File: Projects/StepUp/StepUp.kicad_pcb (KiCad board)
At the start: 2 copper layers, 2 parts, among them U1 TMC2300-LA, U2 RP2040

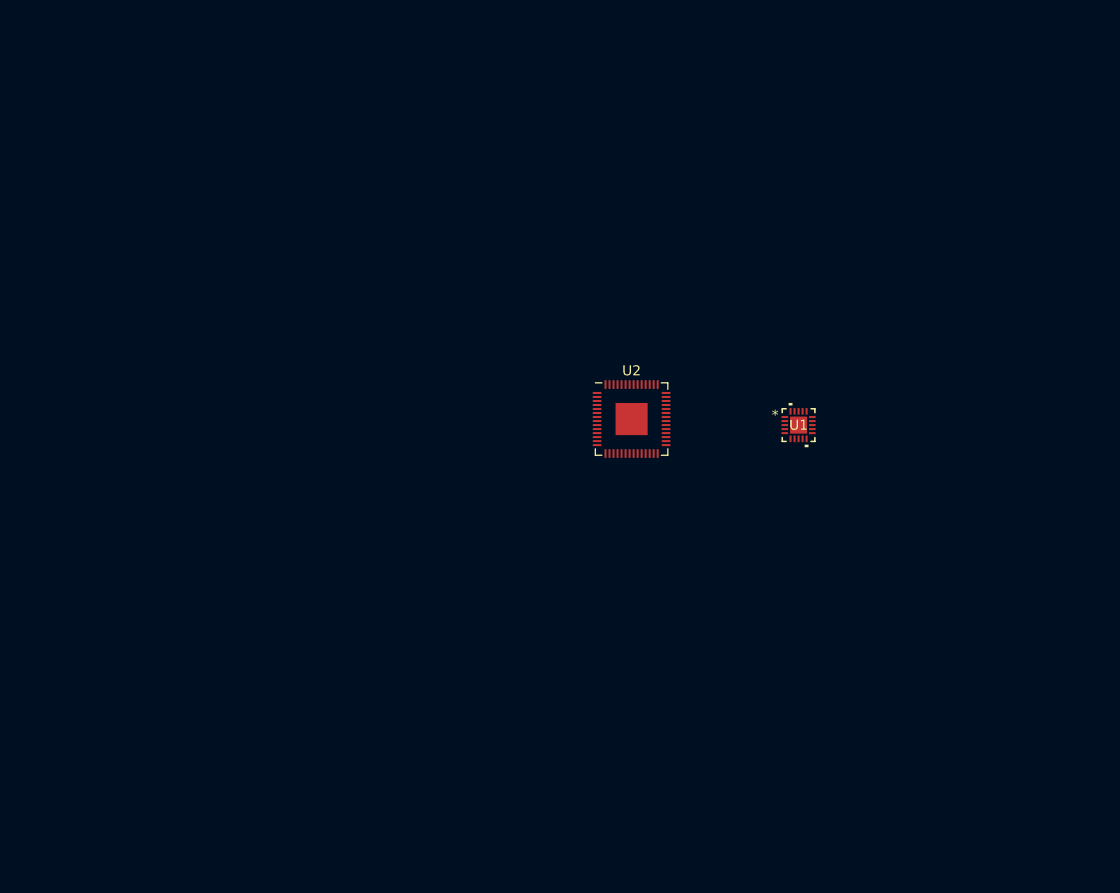
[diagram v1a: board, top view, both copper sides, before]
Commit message: feat(rp2040): Layout begins, extra libraries
RPico minimal project downloaded + assets copied. Boost converter layout
in progress, 18650 battery holder added.
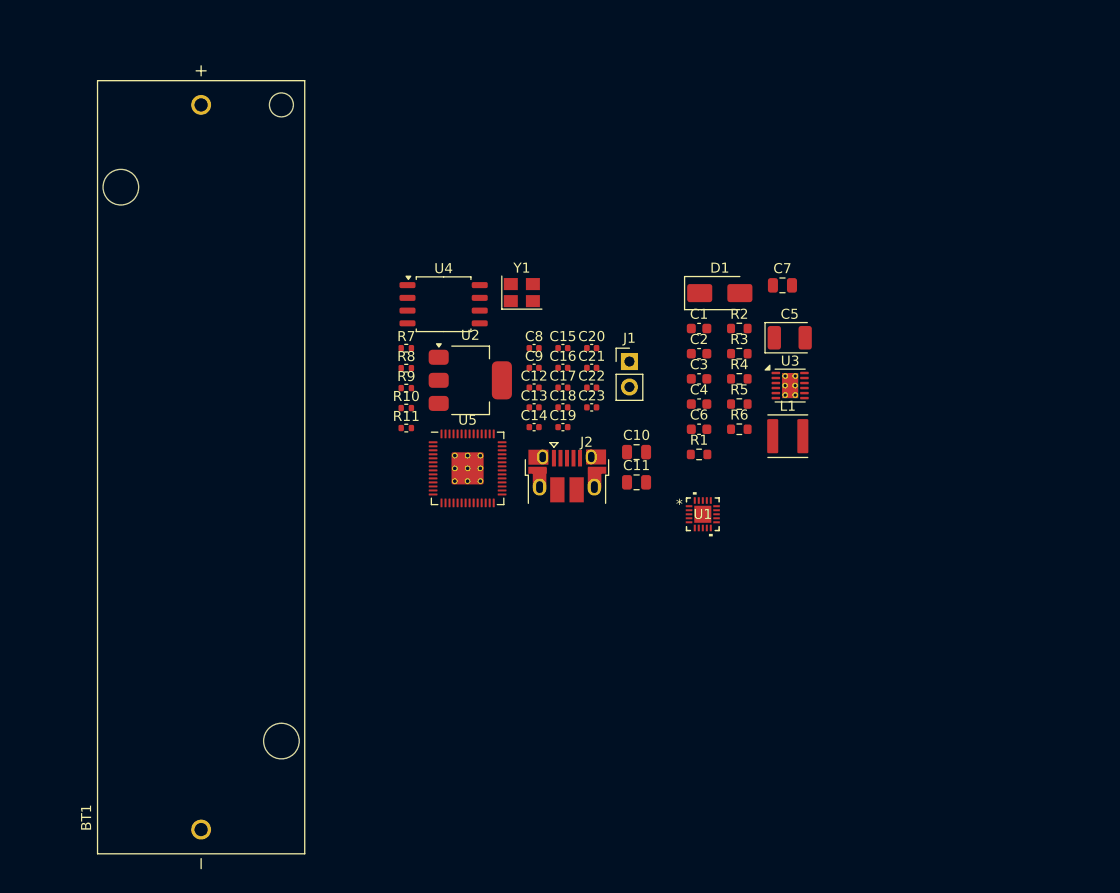
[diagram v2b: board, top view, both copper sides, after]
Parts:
- added BT1: 1043P, Keystone:BAT_1043P, F.Cu at (104.4, 105.0)
- added C1: 0.1uF, Capacitor_SMD:C_0603_1608Metric, F.Cu at (154.0, 91.2)
- added C10: 10u, Capacitor_SMD:C_0805_2012Metric, F.Cu at (147.8, 103.5)
- added C11: 10u, Capacitor_SMD:C_0805_2012Metric, F.Cu at (147.8, 106.5)
- added C12: 100n, Capacitor_SMD:C_0402_1005Metric, F.Cu at (137.6, 97.1)
- added C13: 100n, Capacitor_SMD:C_0402_1005Metric, F.Cu at (137.6, 99.0)
- added C14: 100n, Capacitor_SMD:C_0402_1005Metric, F.Cu at (137.6, 101.0)
- added C15: 1u, Capacitor_SMD:C_0402_1005Metric, F.Cu at (140.4, 93.1)
- added C16: 100n, Capacitor_SMD:C_0402_1005Metric, F.Cu at (140.4, 95.1)
- added C17: 1u, Capacitor_SMD:C_0402_1005Metric, F.Cu at (140.4, 97.1)
- added C18: 100n, Capacitor_SMD:C_0402_1005Metric, F.Cu at (140.4, 99.0)
- added C19: 100n, Capacitor_SMD:C_0402_1005Metric, F.Cu at (140.4, 101.0)
- added C2: 0.01uF, Capacitor_SMD:C_0603_1608Metric, F.Cu at (154.0, 93.7)
- added C20: 100n, Capacitor_SMD:C_0402_1005Metric, F.Cu at (143.3, 93.1)
- added C21: 100n, Capacitor_SMD:C_0402_1005Metric, F.Cu at (143.3, 95.1)
- added C22: 100n, Capacitor_SMD:C_0402_1005Metric, F.Cu at (143.3, 97.1)
- added C23: 100n, Capacitor_SMD:C_0402_1005Metric, F.Cu at (143.3, 99.0)
- added C3: 0.01uF, Capacitor_SMD:C_0603_1608Metric, F.Cu at (154.0, 96.2)
- added C4: 2.2uF, Capacitor_SMD:C_0603_1608Metric, F.Cu at (154.0, 98.7)
- added C5: 100uF, Capacitor_Tantalum_SMD:CP_EIA-3528-12_Kemet-T, F.Cu at (163.1, 92.1)
- added C6: 100pF, Capacitor_SMD:C_0603_1608Metric, F.Cu at (154.0, 101.2)
- added C7: 22uF, Capacitor_SMD:C_0805_2012Metric, F.Cu at (162.3, 86.9)
- added C8: 15p, Capacitor_SMD:C_0402_1005Metric, F.Cu at (137.6, 93.1)
- added C9: 15p, Capacitor_SMD:C_0402_1005Metric, F.Cu at (137.6, 95.1)
- added D1: SK54A-LTP, Diode_SMD:D_SMA, F.Cu at (156.1, 87.6)
- added J1: Conn_01x02, Connector_PinHeader_2.54mm:PinHeader_1x02_P2.54mm_Vertical, F.Cu at (147.1, 94.5)
- added J2: USB_B_Micro, Connector_USB:USB_Micro-B_Amphenol_10103594-0001LF_Horizontal, F.Cu at (140.9, 105.9)
- added L1: 2.2 uH, Inductor_SMD:L_Abracon_ASPI-4030S, F.Cu at (162.9, 101.9)
- added R1: 620R, Resistor_SMD:R_0603_1608Metric, F.Cu at (154.0, 103.7)
- added R10: 27, Resistor_SMD:R_0402_1005Metric, F.Cu at (124.8, 99.1)
- added R11: 1k, Resistor_SMD:R_0402_1005Metric, F.Cu at (124.8, 101.1)
- added R2: 10kR, Resistor_SMD:R_0603_1608Metric, F.Cu at (158.0, 91.2)
- added R3: 9.09kR, Resistor_SMD:R_0603_1608Metric, F.Cu at (158.0, 93.7)
- added R4: 71.5kR, Resistor_SMD:R_0603_1608Metric, F.Cu at (158.0, 96.2)
- added R5: 10kR, Resistor_SMD:R_0603_1608Metric, F.Cu at (158.0, 98.7)
- added R6: 100kR, Resistor_SMD:R_0603_1608Metric, F.Cu at (158.0, 101.2)
- added R7: 1k, Resistor_SMD:R_0402_1005Metric, F.Cu at (124.8, 93.1)
- added R8: DNF, Resistor_SMD:R_0402_1005Metric, F.Cu at (124.8, 95.1)
- added R9: 27, Resistor_SMD:R_0402_1005Metric, F.Cu at (124.8, 97.1)
- added U3: MIC2253, Package_DFN_QFN:DFN-12-1EP_3x3mm_P0.5mm_EP1.6x2.5mm_ThermalVias, F.Cu at (163.1, 96.9)
- added U4: W25Q128JVS, Package_SO:SOIC-8_5.23x5.23mm_P1.27mm, F.Cu at (128.6, 88.8)
- added U5: RP2040, RP2040_minimal_r2:RP2040-QFN-56, F.Cu at (130.9, 105.1)
- added Y1: ABM8-272-T3, Crystal:Crystal_SMD_3225-4Pin_3.2x2.5mm, F.Cu at (136.4, 87.6)
- U2: value RP2040 -> NCP1117-3.3_SOT223; footprint Package_DFN_QFN:QFN-56-1EP_7x7mm_P0.4mm_EP3.2x3.2mm -> Package_TO_SOT_SMD:SOT-223-3_TabPin2
- moved U2 16.5 mm to (131.2, 96.3)
- moved U1 13.0 mm to (154.4, 109.7)
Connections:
- U2 pad 1: Net-(U2-IOVDD-Pad1) -> GND
- U2 pad 2: unconnected-(U2-GPIO0-Pad2) -> +3V3
- U2 pad 3: unconnected-(U2-GPIO1-Pad3) -> VBUS

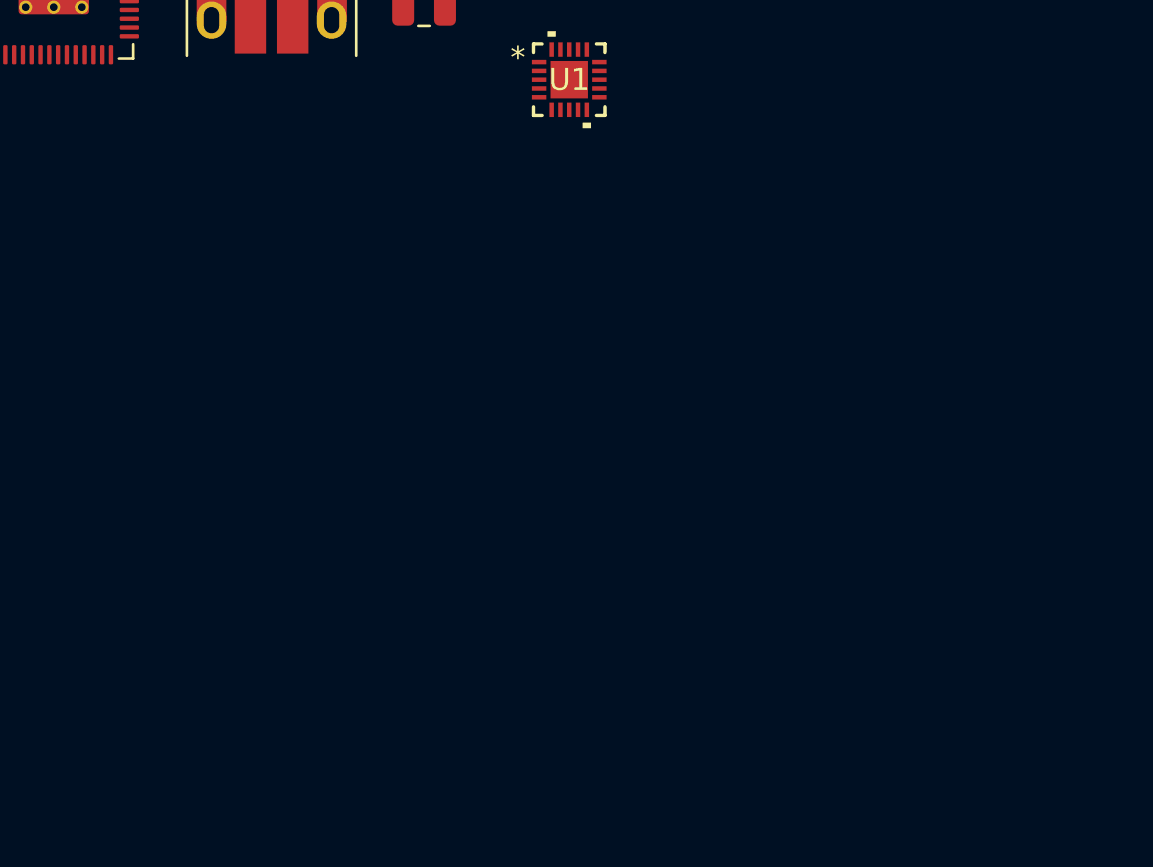
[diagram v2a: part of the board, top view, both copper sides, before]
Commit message: feat(joystick): Added part
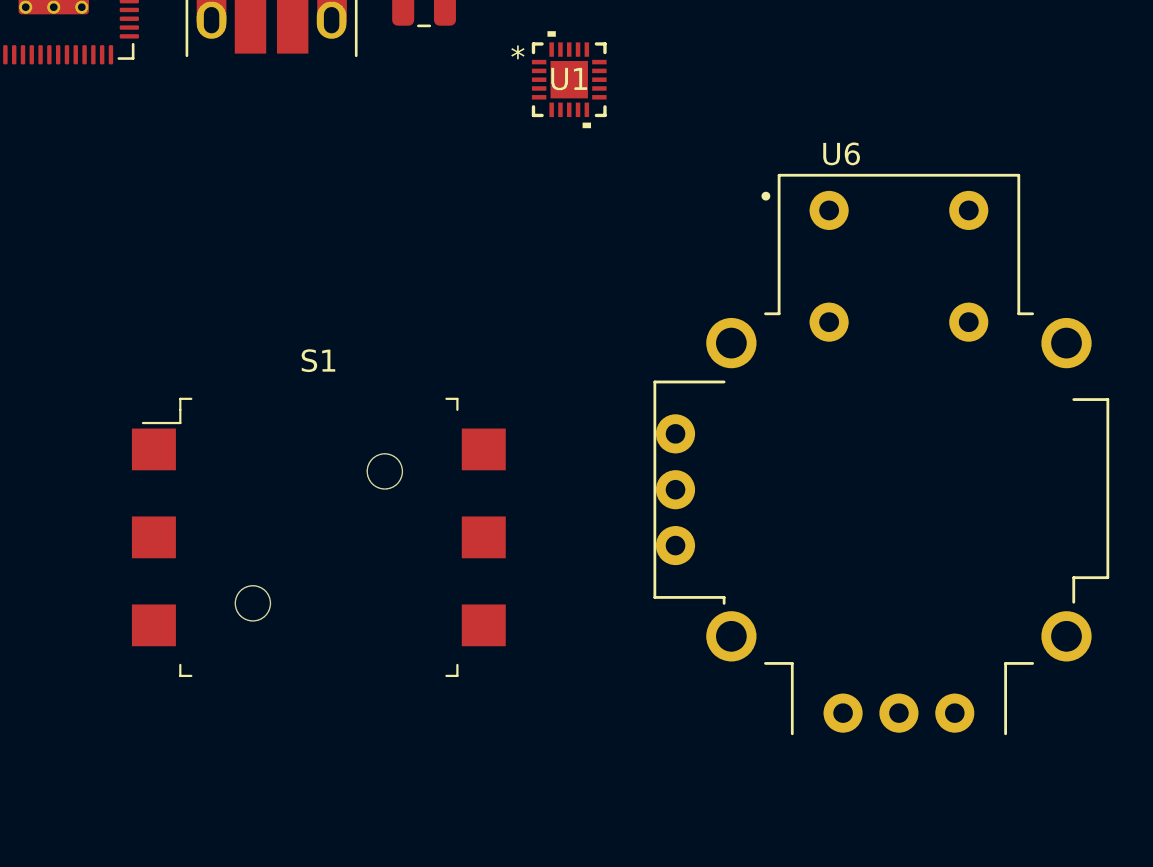
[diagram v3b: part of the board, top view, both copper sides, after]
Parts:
- added S1: JS5208, digikey-footprints:Switch_Nav_12.4x12.4mm_SMD_JS5208, F.Cu at (143.0, 130.5)
- added U6: COM-09032, joystick_footprints:XDCR_COM-09032, F.Cu at (169.4, 128.3)

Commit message: feat(charge): Charge IC, USB ESD, sheet sections
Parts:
- removed S1: JS5208, digikey-footprints:Switch_Nav_12.4x12.4mm_SMD_JS5208
- added C24: 4.7u, Capacitor_SMD:C_0805_2012Metric, F.Cu at (161.1, 112.9)
- added C25: 4.7u, Capacitor_SMD:C_0805_2012Metric, F.Cu at (161.1, 115.9)
- added D2: LED, LED_SMD:LED_0805_2012Metric, F.Cu at (161.1, 118.9)
- added R12: RProg, Resistor_SMD:R_0603_1608Metric, F.Cu at (170.0, 112.6)
- added R13: Rled, Resistor_SMD:R_0603_1608Metric, F.Cu at (170.0, 115.1)
- added U7: MCP73832T-2ACI_OT, digikey-footprints:SOT-753, F.Cu at (165.6, 114.0)
- added U8: USBLC6-2SC6, Package_TO_SOT_SMD:SOT-23-6, F.Cu at (165.9, 119.0)
- moved J2 39.2 mm to (123.5, 141.0), turned to 180 degrees
- moved Y1 25.5 mm to (131.0, 112.5)
- moved U6 25.4 mm to (144.0, 127.5)
- moved U2 23.8 mm to (122.5, 118.5)
- moved C10 7.48 mm to (147.5, 96.0)
- moved C15 7.48 mm to (140.1, 85.6)
- moved C20 7.48 mm to (143.0, 85.6)
- moved R10 7.48 mm to (124.5, 91.6)
- moved R3 7.48 mm to (157.7, 86.2)
- moved R6 7.48 mm to (157.7, 93.7)
- moved R7 7.48 mm to (124.5, 85.7)
- moved R8 7.48 mm to (124.5, 87.6)
- moved U3 7.48 mm to (162.8, 89.4)
- moved C2 7.48 mm to (153.7, 86.2)
- moved C6 7.48 mm to (153.7, 93.7)
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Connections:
- BT1 pad N: unconnected-(BT1-PadN) -> GND
- BT1 pad P: unconnected-(BT1-PadP) -> /Power/Vbat
- J2 pad 2: /Power/USB_D- -> /Power/USB_D-_IN
- J2 pad 3: /Power/USB_D+ -> /Power/USB_D+_IN
